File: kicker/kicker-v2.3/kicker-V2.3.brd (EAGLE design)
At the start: 152.9 x 55 mm, 43 parts, among them IC1 7818TV, IC2 MCP601OT, J1 XT-60BATT_LABEL, Q1 IGB50N60T, Q3 IGB50N60T, U1 LT3750EMSPBF

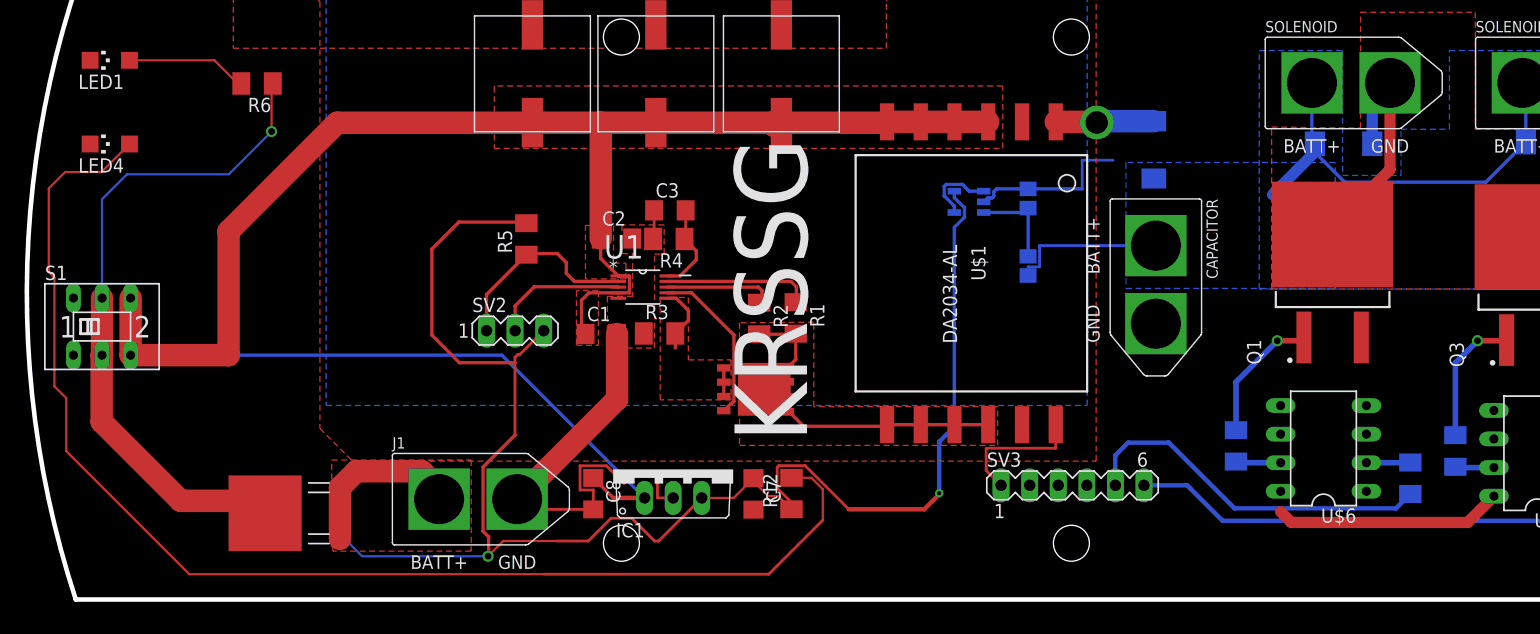
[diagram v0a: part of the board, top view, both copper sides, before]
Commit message: Update Kicker
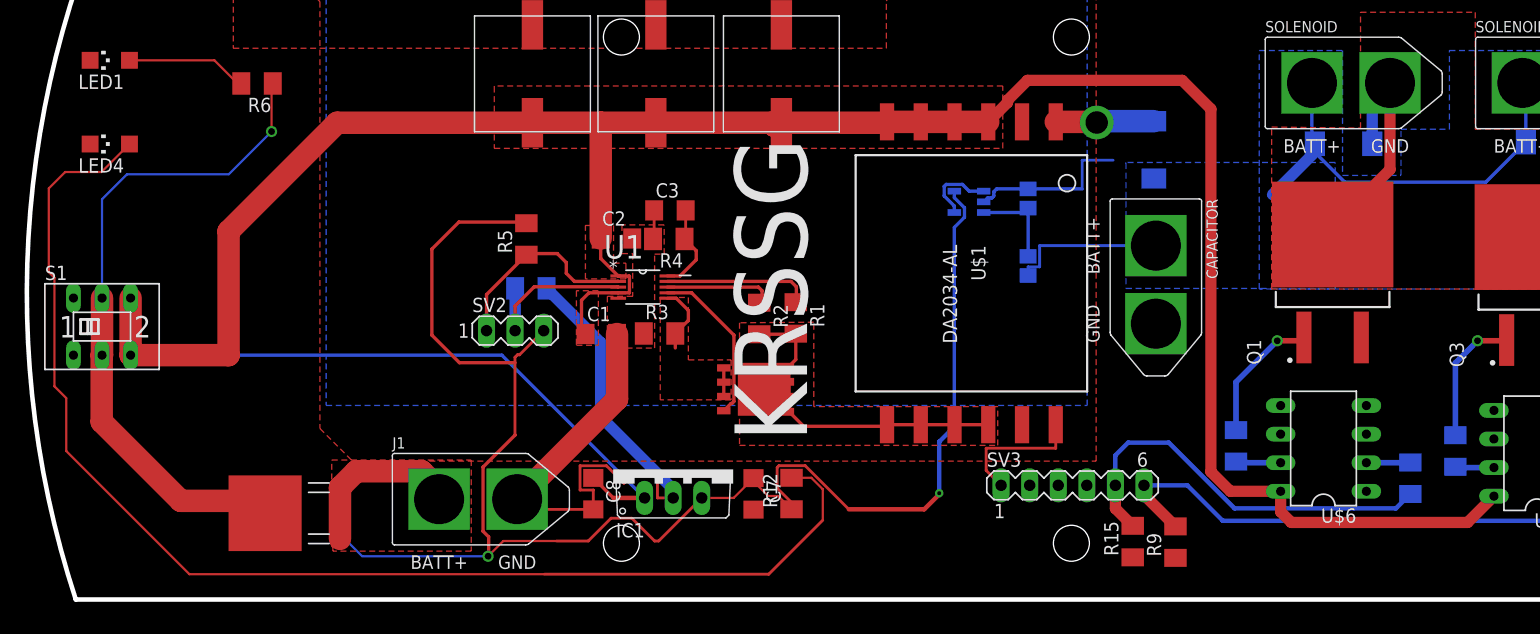
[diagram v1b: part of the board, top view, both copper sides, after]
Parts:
- added R15, R16, R9: 2.49K, resistor:M1206
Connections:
- net CHARGE: now also R16.2
- net GND: now also R15.1, R16.1, R9.1
- net TRIGGER: now also R15.2
- net TRIGGER_CHIP: now also R9.2
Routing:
- net V_TRANS: track 197.8 -> 261.1 mm
- net GND: track 72.5 -> 95.8 mm
- net TRIGGER_CHIP: track 48.6 -> 53.4 mm
- net TRIGGER: track 32.3 -> 36.6 mm
- net CHARGE: track 12.1 -> 15.8 mm
